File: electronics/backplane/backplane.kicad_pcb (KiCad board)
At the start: 4 copper layers, 46 x 100 mm, 43 parts, among them J1 USB_C_SOCKET_RA_PTH_SIMPLE, P1 PAD_SOLDER_2mm, P2 JST_SH_4_RA, P3 JST_SH_4_RA, P4 JST_SH_4_RA, Q1 2N7002P, SW1 B3U-1000P_SPST-NO_SMD, SW2 B3U-1000P_SPST-NO_SMD, U1 USBLC6, U9 AP2112K-3.3, X1 MICROMOD_PROCESSOR_SOCKET, X2 SWD_SMT_SOCKET, X3 MICROMOD_FUNCTION_BOARD_SOCKET

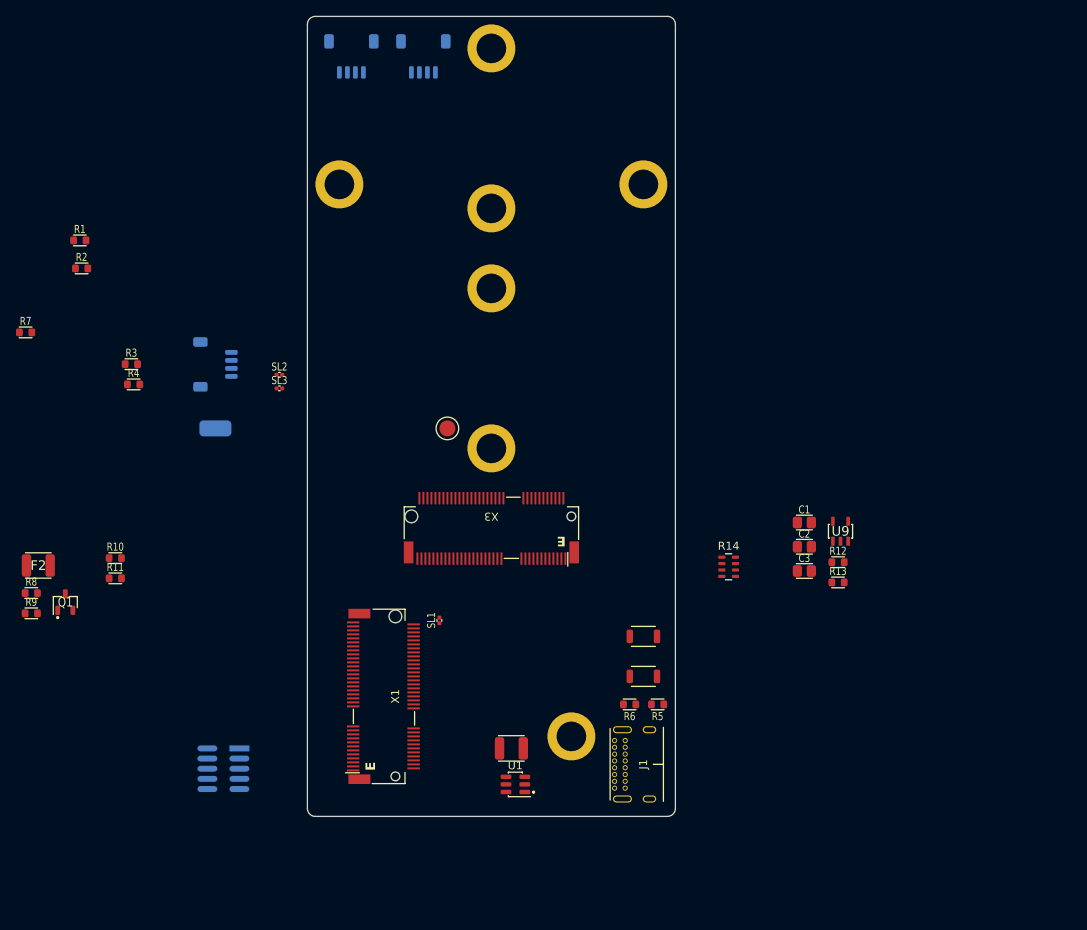
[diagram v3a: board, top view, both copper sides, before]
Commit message: Continue schematic tweaks, start routing backplane
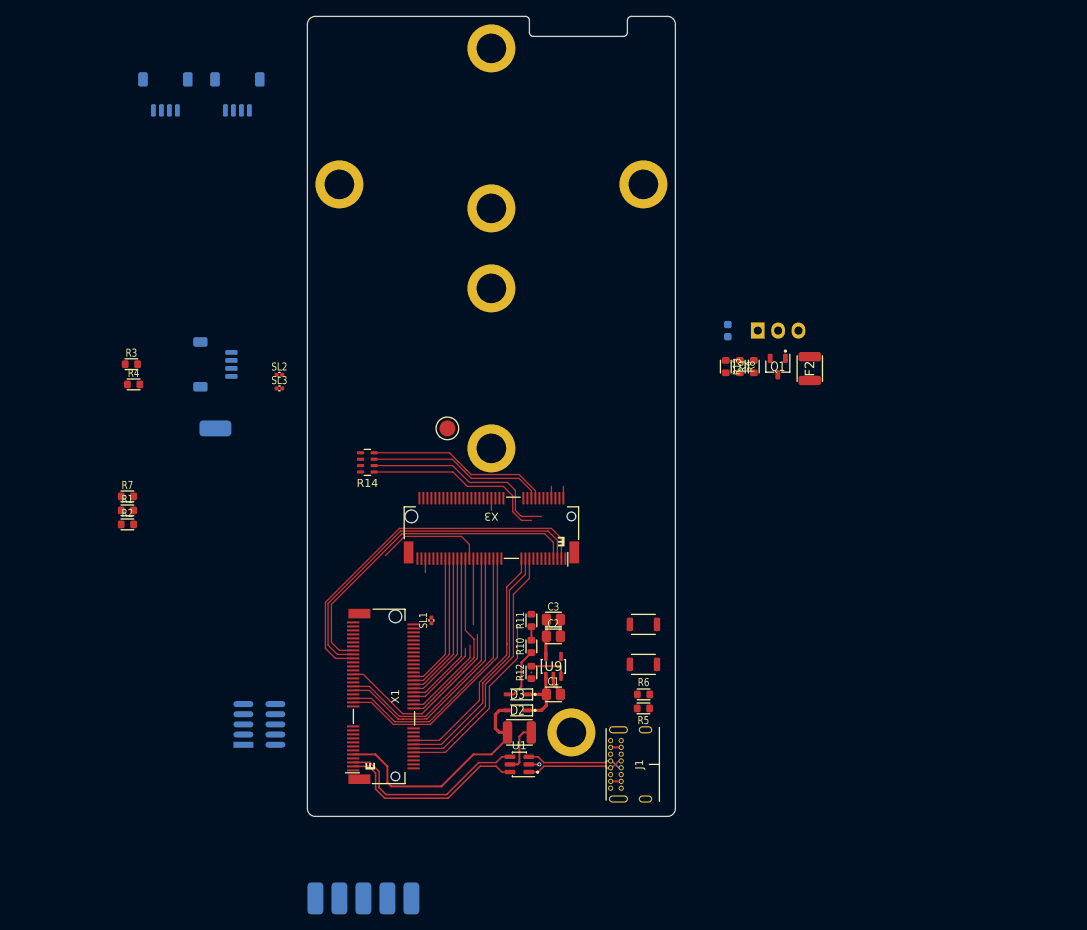
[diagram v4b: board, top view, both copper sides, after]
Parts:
- added D1: LED_YELLOW_1608M, Applidyne_LED:LEDC1608X80L40N, B.Cu at (152.6, 89.3)
- added D2: 40V_500mA_SOD323, Applidyne_SOD:SOD2512X110N, F.Cu at (126.2, 136.8)
- added D3: 40V_500mA_SOD323, Applidyne_SOD:SOD2512X110N, F.Cu at (126.2, 134.8)
- added P10: CONN_01X03, Applidyne_Connector_Wurth:61300311121, B.Cu at (156.3, 89.3)
- added P5: PAD_SOLDER_2mm, Applidyne_Connector:PAD_SOLDER_2mm, B.Cu at (101.0, 160.2)
- added P6: PAD_SOLDER_2mm, Applidyne_Connector:PAD_SOLDER_2mm, B.Cu at (104.0, 160.2)
- added P7: PAD_SOLDER_2mm, Applidyne_Connector:PAD_SOLDER_2mm, B.Cu at (107.0, 160.2)
- added P8: PAD_SOLDER_2mm, Applidyne_Connector:PAD_SOLDER_2mm, B.Cu at (110.0, 160.2)
- added P9: PAD_SOLDER_2mm, Applidyne_Connector:PAD_SOLDER_2mm, B.Cu at (113.0, 160.2)
- R13: value 10R_1608M -> 1K00_1608M
- moved F2 99.5 mm to (162.8, 94.0), turned to 90 degrees
- moved R9 95.4 mm to (155.8, 93.8), turned to 90 degrees
- moved Q1 93.8 mm to (158.8, 93.8), turned to 180 degrees
- moved R8 93.0 mm to (154.1, 93.8), turned to -90 degrees
- moved R10 53.2 mm to (128.0, 128.8), turned to 90 degrees
- moved R11 52.3 mm to (128.0, 125.5), turned to 90 degrees
- moved R14 47.0 mm to (107.5, 105.8), turned to 180 degrees
- moved R12 40.7 mm to (128.0, 132.0), turned to 90 degrees
- moved U9 39.7 mm to (130.8, 131.2)
- moved C1 38.0 mm to (130.8, 134.8)
- moved R1 34.3 mm to (77.5, 111.8)
- moved C2 33.3 mm to (130.8, 127.5)
- moved R2 32.5 mm to (77.5, 113.5)
- moved C3 32.0 mm to (130.8, 125.4)
- moved R13 30.4 mm to (152.3, 93.8), turned to -90 degrees
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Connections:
- F2 pad 2: unconnected-(F2-Pad2) -> Net-(P10-P3)
- J1 pad A4: Net-(J1-VBUS-PadA4) -> Net-(U1-VBUS)
- J1 pad A9: Net-(J1-VBUS-PadA4) -> Net-(U1-VBUS)
- Q1 pad 3: unconnected-(Q1-D-Pad3) -> Net-(P10-P2)
- R13 pad 1: /Power Regulation/CARRIER_PWR_EN -> Net-(D1-PadA)
- R13 pad 2: Net-(U9-EN) -> /Expansion IO/PWM_OUTPUT
- X1 pad 20: /Expansion IO/RX -> unconnected-(X1-UART_RX2-Pad20)
- X1 pad 22: /Expansion IO/TX -> unconnected-(X1-UART_TX2-Pad22)
- X1 pad 50: unconnected-(X1-AUD_BCLK/PCM_CLK/I2S_SCK/PDM_CLK-Pad50) -> Net-(P9-P1)
- X1 pad 52: unconnected-(X1-AUD_LRCLK/PCM_SYNC/I2S_WS/PDM_DATA-Pad52) -> Net-(P8-P1)
- X1 pad 54: unconnected-(X1-AUD_IN/PCM_IN/I2S_IN/CAM_PCLK-Pad54) -> Net-(P7-P1)
- X1 pad 56: unconnected-(X1-AUD_OUT/PCM_OUT/I2S_OUT/CAM_MCLK-Pad56) -> Net-(P6-P1)
- X1 pad 58: unconnected-(X1-AUD_MCLK-Pad58) -> Net-(P5-P1)
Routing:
- net /Function Board/CLK: track 0.00 -> 46.1 mm
- net /Function Board/COPI: track 0.00 -> 44.0 mm
- net /Function Board/CIPO: track 0.00 -> 41.8 mm
- net /Function Board/D+: track 0.00 -> 35.0 mm
- net /Function Board/D-: track 0.00 -> 34.4 mm
- net /Function Board/CAN.RX: track 0.00 -> 33.8 mm
- net /Function Board/CAN.TX: track 0.00 -> 33.2 mm
- net /Function Board/FN_~{INT}: track 0.00 -> 31.9 mm
- net /Expansion IO/I2C0.SDA: track 0.00 -> 31.9 mm
- net /Expansion IO/I2C0.SCL: track 0.00 -> 31.0 mm
- net /Power Regulation/USB_VCC: track 0.00 -> 30.6 mm
- net /Expansion IO/~{I2C_INT}: track 0.00 -> 30.4 mm
- net Net-(X1-BATT_VIN/3): track 0.00 -> 25.1 mm
- net Net-(X3-FUNC_TX): track 0.00 -> 25.0 mm
- net /Processor/NATIVE.D-: track 0.00 -> 24.4 mm
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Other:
- outline, holes or cut-outs redrawn

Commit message: Continue backplane design Cleanup schematic, most routing and placement done
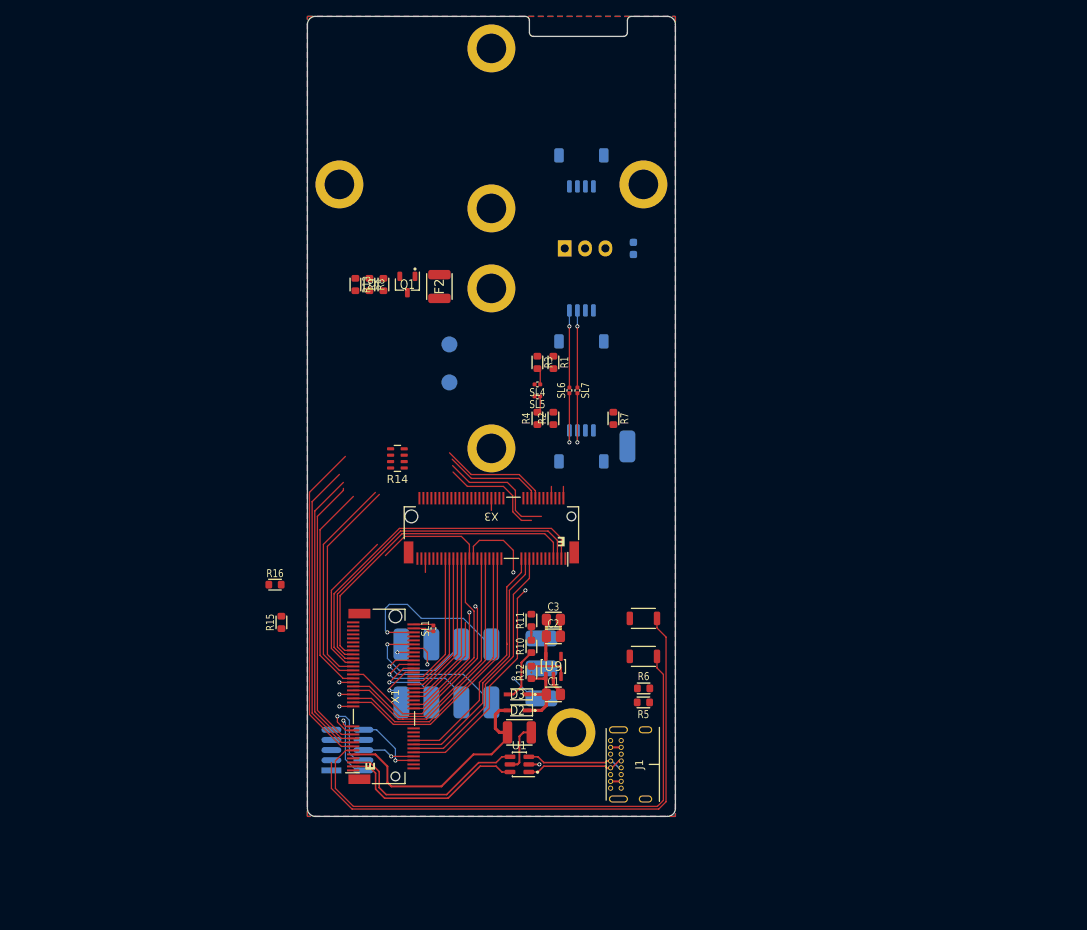
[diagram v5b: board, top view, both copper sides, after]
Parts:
- removed SL2, SL3: SOLDER-LINK-2-TINY, Applidyne_Link:SJ1005-2N
- added P11: PAD_SOLDER_2mm, Applidyne_Connector:PAD_SOLDER_2mm, B.Cu at (111.8, 128.5)
- added P12: PAD_SOLDER_2mm, Applidyne_Connector:PAD_SOLDER_2mm, B.Cu at (119.2, 128.5)
- added P13: PAD_SOLDER_2mm, Applidyne_Connector:PAD_SOLDER_2mm, B.Cu at (115.5, 128.5)
- added P14: PAD_SOLDER_2mm, Applidyne_Connector:PAD_SOLDER_2mm, B.Cu at (123.0, 128.5)
- added P15: PAD_SOLDER_2mm, Applidyne_Connector:PAD_SOLDER_2mm, B.Cu at (129.2, 127.8)
- added P16: PAD_SOLDER_2mm, Applidyne_Connector:PAD_SOLDER_2mm, B.Cu at (129.2, 131.5)
- added R15: 100K_1608M, Applidyne_Resistor:RESC1608X50N, F.Cu at (96.8, 125.8)
- added R16: 100K_1608M, Applidyne_Resistor:RESC1608X50N, F.Cu at (96.0, 121.0)
- added SL4: SOLDER-LINK-2-TINY, Applidyne_Link:SJ1005-2N, F.Cu at (128.8, 96.0)
- added SL5: SOLDER-LINK-2-TINY, Applidyne_Link:SJ1005-2N, F.Cu at (128.8, 97.5)
- added SL6: SOLDER-LINK-2-TINY, Applidyne_Link:SJ1005-2N, F.Cu at (132.8, 96.8)
- added SL7: SOLDER-LINK-2-TINY, Applidyne_Link:SJ1005-2N, F.Cu at (133.8, 96.8)
- added TEST1: PROBE_PAD, Applidyne_Test:TP200, B.Cu at (117.8, 95.8)
- TEST2: moved to B.Cu
- moved R7 61.5 mm to (138.2, 100.2), turned to -90 degrees
- moved R1 56.4 mm to (130.8, 93.2), turned to -90 degrees
- moved R2 54.9 mm to (130.8, 100.2), turned to 90 degrees
- moved P2 52.9 mm to (134.2, 69.2)
- moved P3 51.9 mm to (134.2, 88.8), turned to 180 degrees
- moved P1 51.5 mm to (140.0, 103.8), turned to 0 degrees
- moved R3 50.8 mm to (128.8, 93.2), turned to -90 degrees
- moved R4 50.7 mm to (128.8, 100.2), turned to 90 degrees
- moved F2 47.4 mm to (116.5, 83.8)
- moved Q1 47.4 mm to (112.5, 83.5)
- moved R13 47.4 mm to (106.0, 83.5)
- moved R8 47.4 mm to (107.8, 83.5)
- moved R9 47.4 mm to (109.5, 83.5)
- moved P4 46.9 mm to (134.2, 103.8), turned to 180 degrees
- moved P5 37.7 mm to (129.2, 135.2), turned to -90 degrees
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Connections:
- P5 pad 1: Net-(P5-P1) -> +POWER
- X1 pad 47: /Processor/PWM1 -> /Expansion IO/PWM_OUTPUT
- X1 pad 51: /Expansion IO/I2C1.SDA -> Net-(X1-I2C_SDA1)
- X1 pad 53: /Expansion IO/I2C1.SCL -> Net-(X1-I2C_SCL1)
- X1 pad 58: Net-(P5-P1) -> unconnected-(X1-AUD_MCLK-Pad58)
- X1 pad 60: /Processor/SPI1.CLK -> /Expansion IO/CLK
- X1 pad 62: /Processor/SPI1.COPI -> /Expansion IO/COPI
- X1 pad 64: /Processor/SPI1.CIPO -> /Expansion IO/CIPO
- X1 pad 70: /Processor/SPI1.~{CS} -> /Expansion IO/~{CS}
- X3 pad 71: /Function Board/FN_PWR_EN -> Net-(TEST1-PAD)
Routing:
- net /Processor/~{RESET}: track 0.00 -> 78.7 mm, vias 0 -> 1
- net /Processor/~{BOOT}: track 0.00 -> 66.8 mm
- net /Function Board/RTS: track 0.00 -> 41.2 mm
- net /Function Board/CTS: track 0.00 -> 37.9 mm
- net /Function Board/TX: track 0.00 -> 36.3 mm
- net /Function Board/RX: track 0.00 -> 34.8 mm
- net Net-(X1-I2C_SDA1): track 0.00 -> 27.5 mm
- net /Expansion IO/PWM_OUTPUT: track 0.00 -> 26.9 mm
- net Net-(X1-I2C_SCL1): track 0.00 -> 26.5 mm
- net /Expansion IO/~{CS}: track 0.00 -> 21.9 mm, vias 0 -> 1
- net /Function Board/~{CS}: track 13.7 -> 32.5 mm
- net Net-(P6-P1): track 0.00 -> 17.9 mm, vias 0 -> 1
- net /Expansion IO/CIPO: track 0.00 -> 16.2 mm, vias 0 -> 1
- net Net-(P7-P1): track 0.00 -> 14.6 mm, vias 0 -> 1
- net /Expansion IO/I2C1.SDA: track 0.00 -> 11.8 mm, vias 0 -> 1
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- added copper zone on B.Cu, net GND
- added copper zone on F.Cu, net GND
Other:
- copper layers 4 -> 2

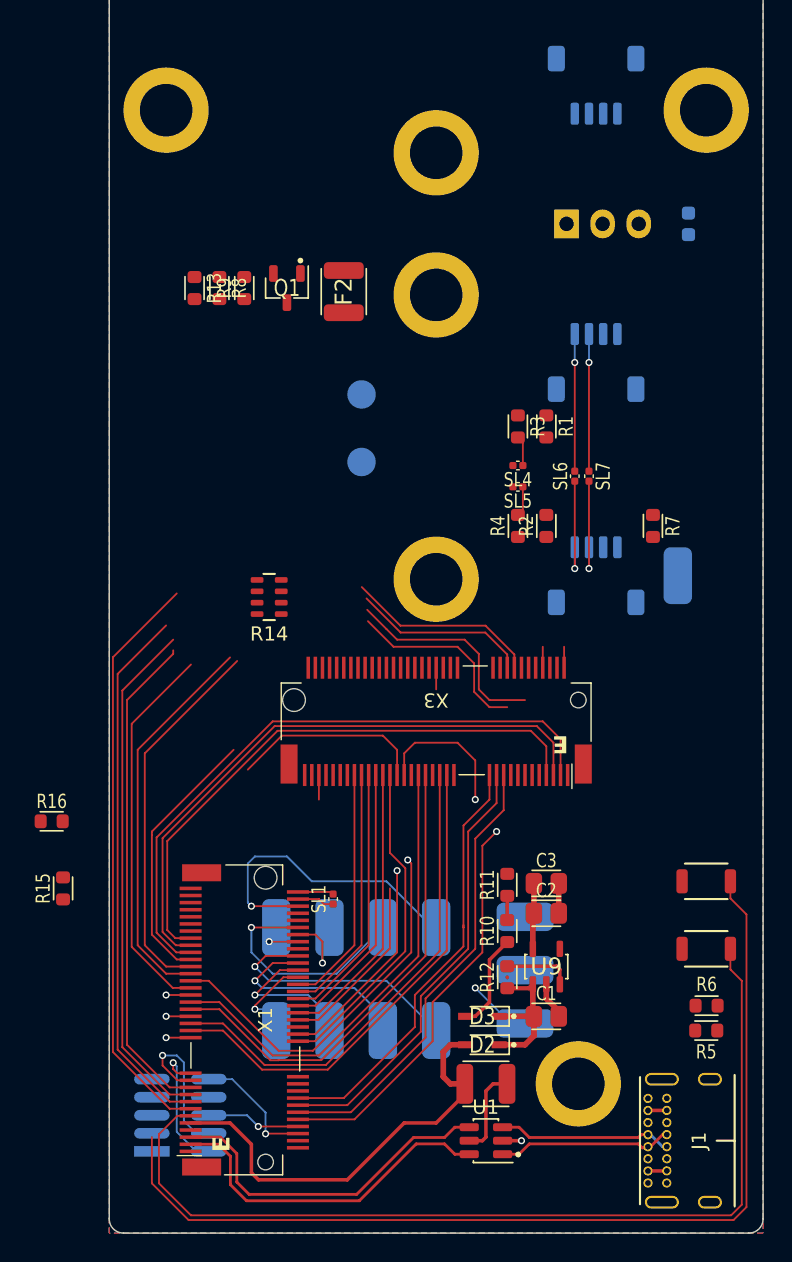
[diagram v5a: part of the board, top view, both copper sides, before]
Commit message: Continued routing Labels, most traces, most pours
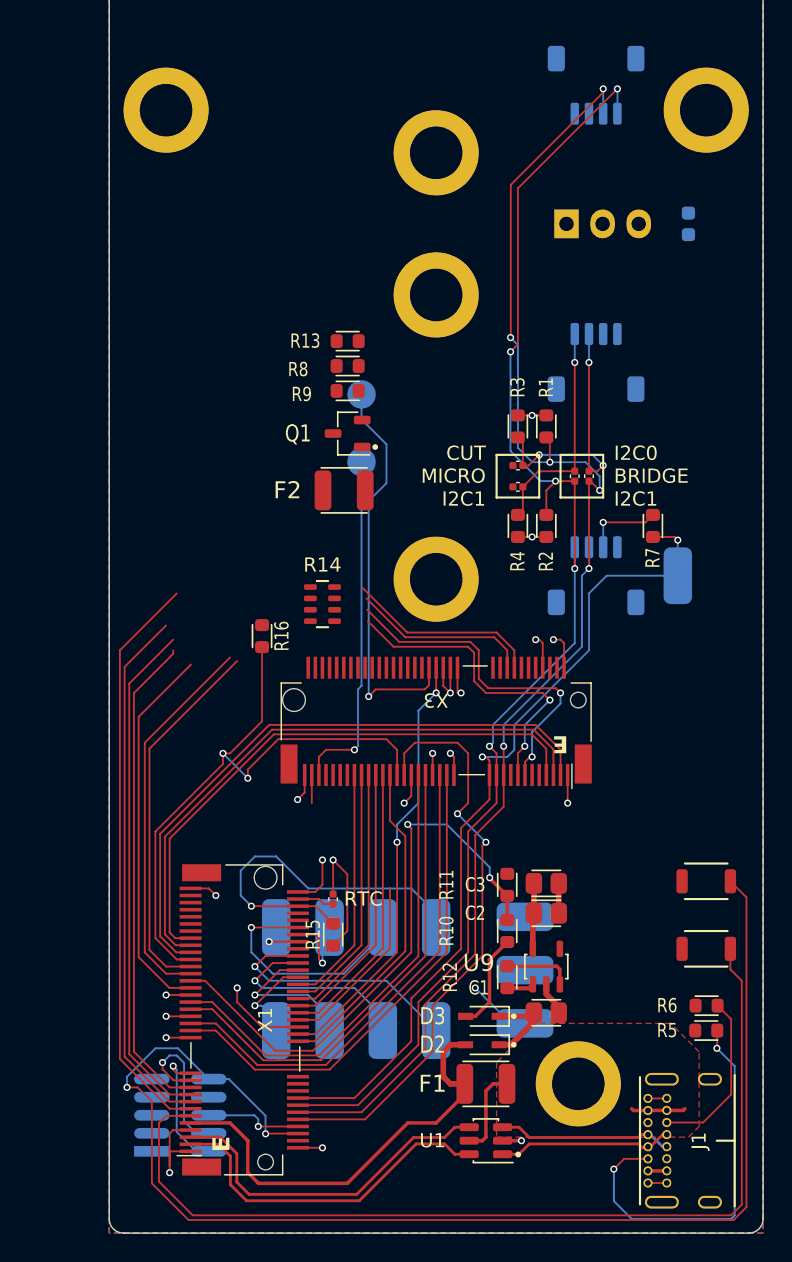
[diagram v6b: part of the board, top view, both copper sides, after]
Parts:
- moved R16 19.7 mm to (110.8, 108.0), turned to -90 degrees
- moved R15 19.3 mm to (115.8, 129.0)
- moved F2 14.0 mm to (116.5, 97.8), turned to 0 degrees
- moved R13 11.4 mm to (116.8, 87.2), turned to 180 degrees
- moved Q1 11.1 mm to (116.8, 93.8), turned to 90 degrees
- moved R8 10.6 mm to (116.8, 89.0), turned to 180 degrees
- moved R9 10.3 mm to (116.8, 90.8), turned to 0 degrees
- moved R14 3.78 mm to (115.0, 105.8)
- moved C1 0.25 mm to (130.8, 134.5)
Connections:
- net /Processor/ADC1 renamed /Expansion IO/ANALOG_IN
- net /Processor/D1 renamed /Expansion IO/DIGITAL_OUT
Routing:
- net /Expansion IO/I2C0.SDA: track 39.6 -> 97.4 mm, vias 1 -> 6
- net /Expansion IO/I2C0.SCL: track 38.7 -> 94.7 mm, vias 1 -> 5
- net GND: track 14.2 -> 48.7 mm, vias 4 -> 16
- net /Expansion IO/~{I2C_INT}: track 30.4 -> 59.0 mm, vias 0 -> 2
- net Net-(TEST2-PAD): track 0.00 -> 28.3 mm, vias 0 -> 1
- net Net-(J1-CC1): track 0.00 -> 27.6 mm, vias 0 -> 2
- net +3.3V: track 7.17 -> 31.0 mm, vias 0 -> 6
- net Net-(TEST1-PAD): track 1.72 -> 24.4 mm, vias 0 -> 1
- net /Function Board/FN_ANALOG: track 16.6 -> 30.5 mm, vias 1 -> 2
- net /Processor/~{RESET}: track 78.7 -> 91.4 mm, vias 1 -> 2
- net Net-(X1-BATT_VIN/3): track 28.7 -> 40.8 mm, vias 1 -> 2
- net Net-(J1-CC2): track 0.00 -> 12.0 mm
- net /Function Board/~{CS}: track 32.5 -> 43.5 mm, vias 0 -> 2
- net Net-(X3-FUNC_RX): track 13.5 -> 22.5 mm, vias 0 -> 2
- net Net-(X3-FUNC_TX): track 15.2 -> 24.1 mm, vias 0 -> 2
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- added copper zone on F.Cu, net Net-(U1-VBUS)
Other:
- board text added: "3V3"
- board text added: "50"
- board text added: "52"
- board text added: "54"
- board text added: "56"
- board text added: "CIPO"
- board text added: "CLK"
- board text added: "COPI"
- board text added: "CUT MICRO I2C1"
- board text added: "FN PWR ENABLE"
- board text added: "GND"
- board text added: "I2C0"
- board text added: "I2C0 BRIDGE I2C1"
- board text added: "I2C1"
- board text added: "PWM"
- board text added: "PWR"
- board text added: "RTC"
- board text added: "WP"
- board text added: "~{CS}"
- board text added: "~{INT}"
